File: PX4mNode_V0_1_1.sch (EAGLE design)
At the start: 128 parts, among them J201 DF13C-6P-1.25V, J202 DF13C-6P-1.25V, J203 DF13C-6P-1.25V, J301 DF13C-4P-1.25V, J401 DF13C-7P-1.25V, J402 DF13-4P-1.25V, J403 DF13C-4P-1.25V, J404 DF13C-4P-1.25V, J405 DF13C-4P-1.25V, J801 DF13C-3P-1.25V, M3_MOUNT1101 MOUNT-HOLE3.1MM, M3_MOUNT1102 MOUNT-HOLE3.1MM, M3_MOUNT1103 MOUNT-HOLE3.1MM, M3_MOUNT1104 MOUNT-HOLE3.1MM, U101 STM32F4X7VX, U401 MAX3051, U402 MAX3051, X101 3.2x2.5 mm / 24 MHz / 15 ppm

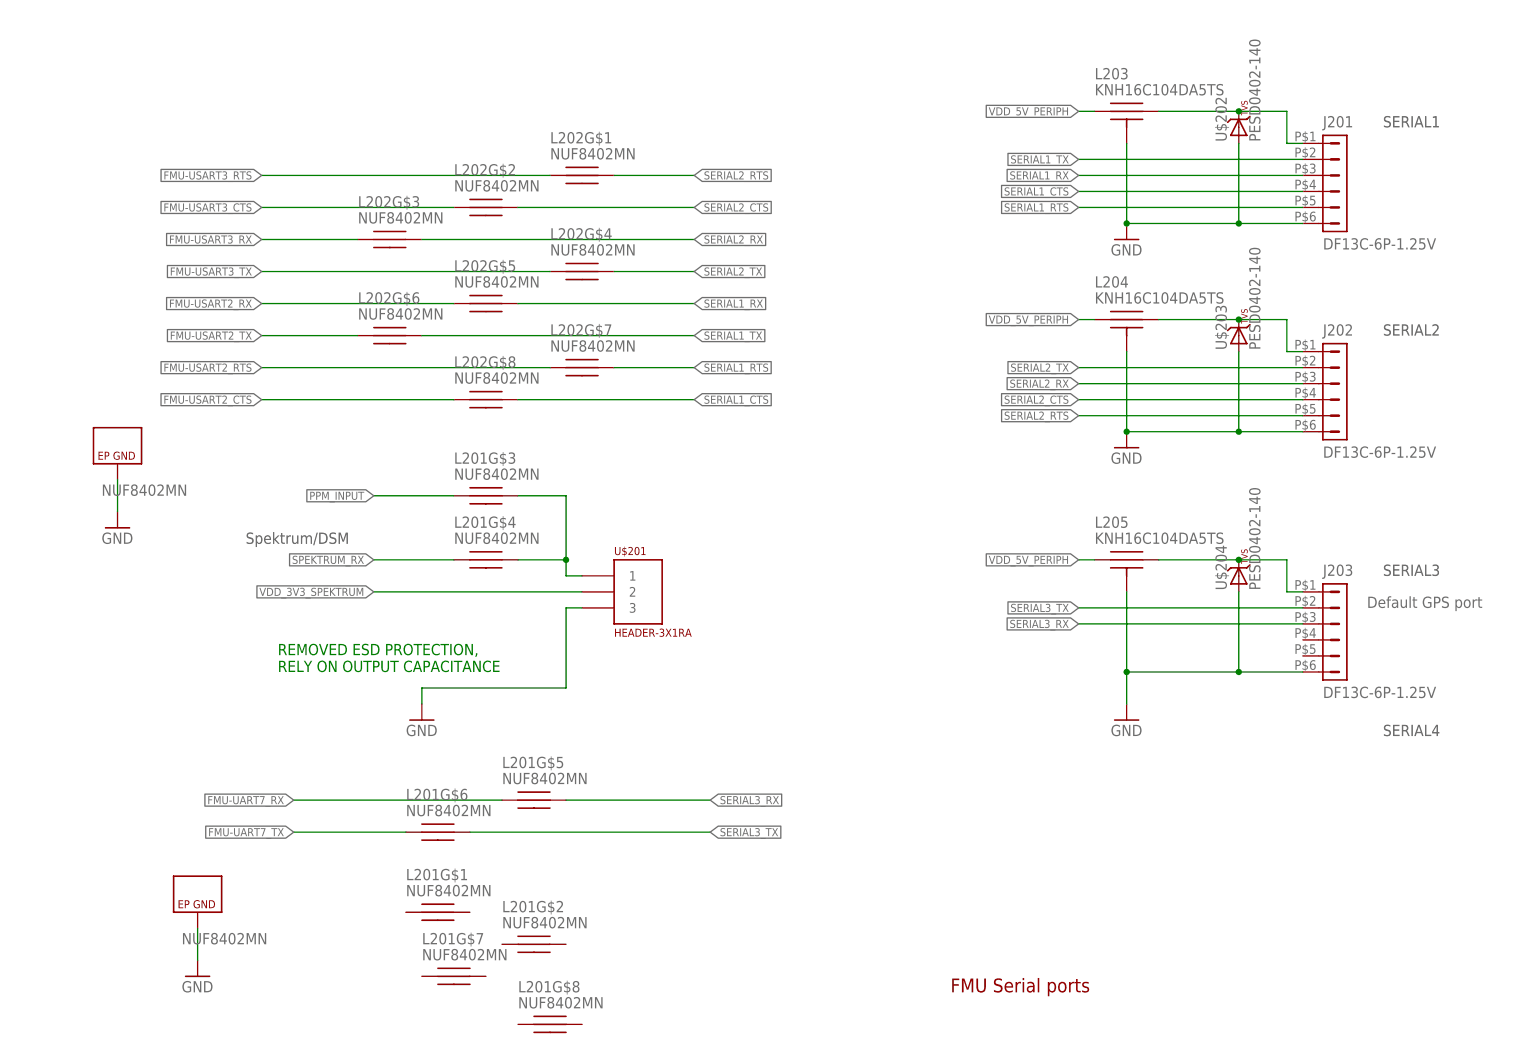
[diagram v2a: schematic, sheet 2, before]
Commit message: Added spektrum 3V3 enable signal
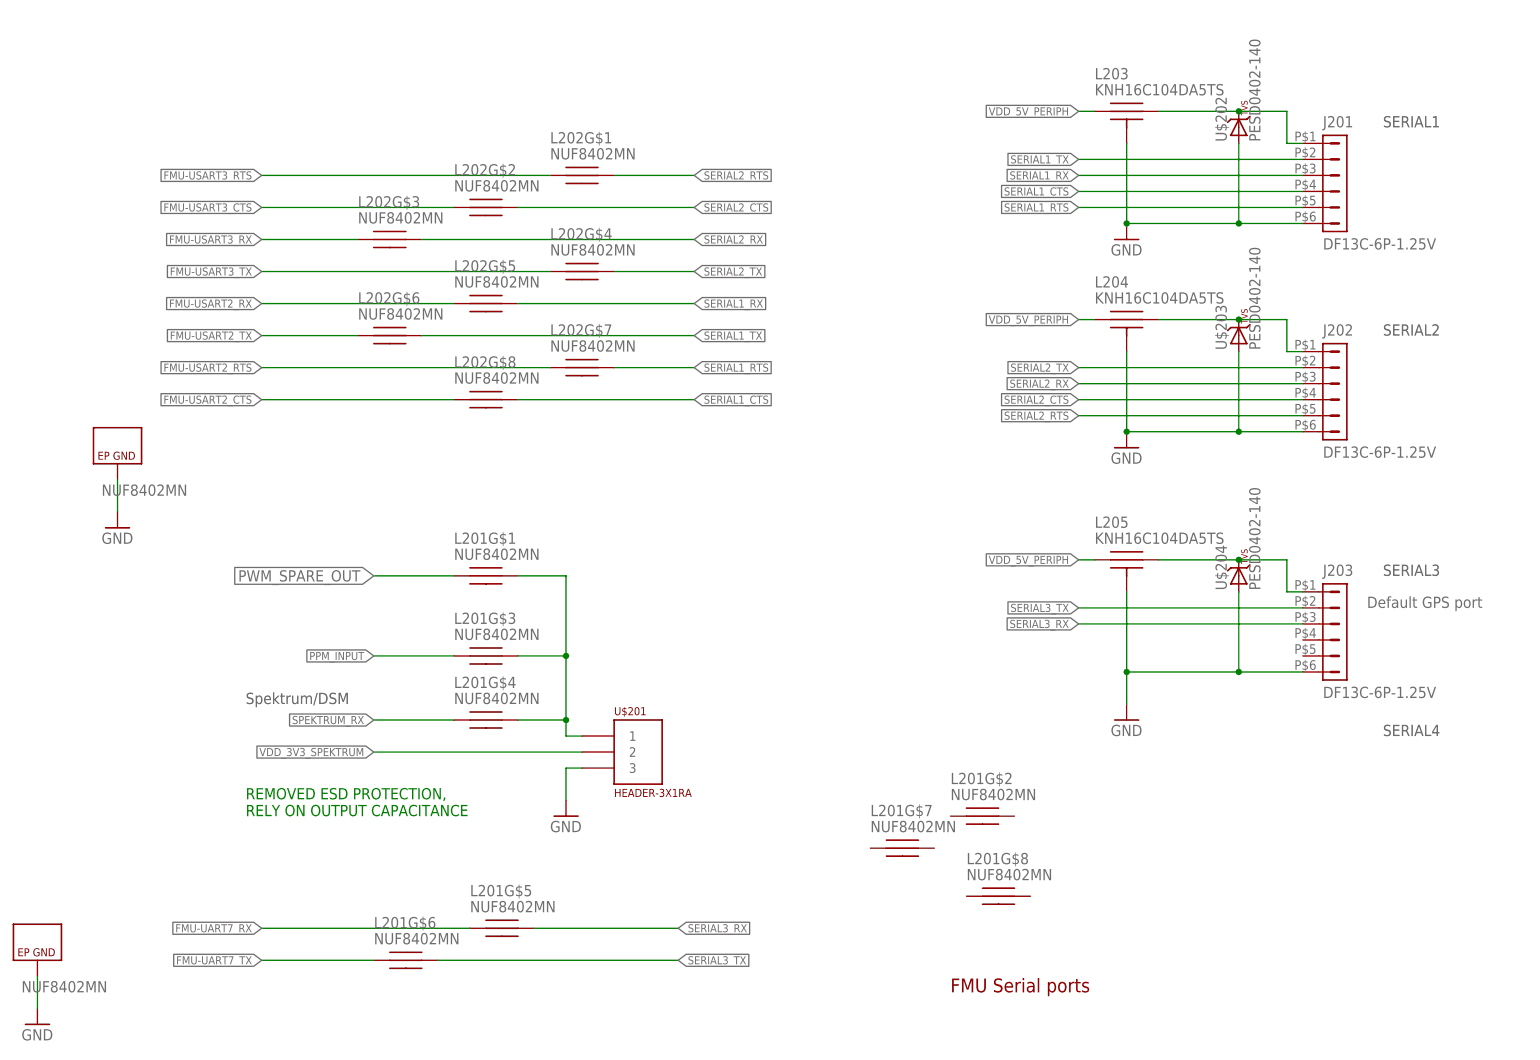
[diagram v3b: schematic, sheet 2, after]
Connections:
- removed net FMU-CH10: U101PORTA_L.PA3
- new net PWM_SPARE_OUT: L201G$1.P$1
- net N$18: now also L201G$1.P$2
- net VDD_3V3_SPEKTRUM_EN: now also U101PORTA_L.PA3
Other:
- note added: "FMU-CH10 changed to Spektrum 3v3 EN"
- moved on the sheet: L201G$1, L201G$2, L201G$3, L201G$4, L201G$5, L201G$6, L201G$7, L201G$8, U$201
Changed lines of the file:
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@@
 <text x="112.014" y="159.512" size="1.27" layer="91">Spare ADC</text>
 <text x="112.014" y="162.052" size="1.27" layer="91">Spare ADC</text>
+<text x="68.58" y="160.02" size="1.27" layer="91">FMU-CH10 changed to
+Spektrum 3v3 EN</text>
 </plain>
 <instances>
@@
 </segment>
 </net>
-<net name="FMU-CH10" class="0">
+<net name="VDD_3V3_SPEKTRUM_EN" class="0">
 <segment>
 <pinref part="U101" gate="PORTA_L" pin="PA3"/>
-<wire x1="33.02" y1="157.48" x2="53.34" y2="157.48" width="0.1524" layer="91"/>
-<label x="53.34" y="157.48" size="1.27" layer="95" xref="yes"/>
+<wire x1="33.02" y1="157.48" x2="40.64" y2="157.48" width="0.1524" layer="91"/>
+<label x="40.64" y="157.48" size="1.27" layer="95" xref="yes"/>
 </segment>
 </net>
@@
 <text x="233.68" y="58.42" size="1.778" layer="97">SERIAL4</text>
 <text x="231.14" y="78.74" size="1.778" layer="95">Default GPS port</text>
-<text x="53.34" y="88.9" size="1.778" layer="97">Spektrum/DSM</text>
-<text x="58.42" y="68.58" size="1.778" layer="91">REMOVED ESD PROTECTION,
+<text x="53.34" y="63.5" size="1.778" layer="97">Spektrum/DSM</text>
+<text x="53.34" y="45.72" size="1.778" layer="91">REMOVED ESD PROTECTION,
 RELY ON OUTPUT CAPACITANCE</text>
 </plain>
@@
 <instance part="L202" gate="G$9" x="33.02" y="99.06"/>
 <instance part="GND8" gate="1" x="33.02" y="91.44"/>
-<instance part="L201" gate="G$9" x="45.72" y="27.94"/>
-<instance part="L201" gate="G$5" x="99.06" y="48.26"/>
-<instance part="L201" gate="G$6" x="83.82" y="43.18"/>
-<instance part="L201" gate="G$3" x="91.44" y="96.52"/>
-<instance part="L201" gate="G$4" x="91.44" y="86.36"/>
-<instance part="GND9" gate="1" x="45.72" y="20.32"/>
-<instance part="GND46" gate="1" x="81.28" y="60.96"/>
-<instance part="U$201" gate="G$1" x="114.3" y="78.74"/>
-<instance part="L201" gate="G$1" x="83.82" y="30.48"/>
-<instance part="L201" gate="G$2" x="99.06" y="25.4"/>
-<instance part="L201" gate="G$7" x="86.36" y="20.32"/>
-<instance part="L201" gate="G$8" x="101.6" y="12.7"/>
+<instance part="L201" gate="G$9" x="20.32" y="20.32"/>
+<instance part="L201" gate="G$5" x="93.98" y="27.94"/>
+<instance part="L201" gate="G$6" x="78.74" y="22.86"/>
+<instance part="L201" gate="G$3" x="91.44" y="71.12"/>
+<instance part="L201" gate="G$4" x="91.44" y="60.96"/>
+<instance part="GND9" gate="1" x="20.32" y="12.7"/>
+<instance part="GND46" gate="1" x="104.14" y="45.72"/>
+<instance part="U$201" gate="G$1" x="114.3" y="53.34"/>
+<instance part="L201" gate="G$1" x="91.44" y="83.82"/>
+<instance part="L201" gate="G$2" x="170.18" y="45.72"/>
+<instance part="L201" gate="G$7" x="157.48" y="40.64"/>
+<instance part="L201" gate="G$8" x="172.72" y="33.02"/>
 </instances>
 <busses>
@@
 </segment>
 <segment>
-<label x="127" y="43.18" size="1.27" layer="95" xref="yes"/>
+<label x="121.92" y="22.86" size="1.27" layer="95" xref="yes"/>
 <pinref part="L201" gate="G$6" pin="P$2"/>
-<wire x1="127" y1="43.18" x2="88.9" y2="43.18" width="0.1524" layer="91"/>
+<wire x1="121.92" y1="22.86" x2="83.82" y2="22.86" width="0.1524" layer="91"/>
 </segment>
 </net>
@@
 </segment>
 <segment>
-<label x="127" y="48.26" size="1.27" layer="95" xref="yes"/>
+<label x="121.92" y="27.94" size="1.27" layer="95" xref="yes"/>
 <pinref part="L201" gate="G$5" pin="P$2"/>
-<wire x1="127" y1="48.26" x2="104.14" y2="48.26" width="0.1524" layer="91"/>
+<wire x1="121.92" y1="27.94" x2="99.06" y2="27.94" width="0.1524" layer="91"/>
 </segment>
 </net>
@@
 <segment>
 <pinref part="GND9" gate="1" pin="GND"/>
-<wire x1="45.72" y1="22.86" x2="45.72" y2="27.94" width="0.1524" layer="91"/>
+<wire x1="20.32" y1="15.24" x2="20.32" y2="20.32" width="0.1524" layer="91"/>
 <pinref part="L201" gate="G$9" pin="GND"/>
 </segment>
@@
 <pinref part="GND46" gate="1" pin="GND"/>
 <pinref part="U$201" gate="G$1" pin="3"/>
-<wire x1="81.28" y1="66.04" x2="81.28" y2="63.5" width="0.1524" layer="91"/>
-<wire x1="106.68" y1="78.74" x2="104.14" y2="78.74" width="0.1524" layer="91"/>
-<wire x1="104.14" y1="78.74" x2="104.14" y2="66.04" width="0.1524" layer="91"/>
-<wire x1="104.14" y1="66.04" x2="81.28" y2="66.04" width="0.1524" layer="91"/>
+<wire x1="106.68" y1="53.34" x2="104.14" y2="53.34" width="0.1524" layer="91"/>
+<wire x1="104.14" y1="53.34" x2="104.14" y2="48.26" width="0.1524" layer="91"/>
 </segment>
 </net>
@@
 <net name="SPEKTRUM_RX" class="0">
 <segment>
-<label x="73.66" y="86.36" size="1.27" layer="95" font="vector" rot="R180" xref="yes"/>
-<wire x1="86.36" y1="86.36" x2="73.66" y2="86.36" width="0.1524" layer="91"/>
+<label x="73.66" y="60.96" size="1.27" layer="95" font="vector" rot="R180" xref="yes"/>
+<wire x1="86.36" y1="60.96" x2="73.66" y2="60.96" width="0.1524" layer="91"/>
 <pinref part="L201" gate="G$4" pin="P$1"/>
 </segment>
@@
 <net name="VDD_3V3_SPEKTRUM" class="1">
 <segment>
-<label x="73.66" y="81.28" size="1.27" layer="95" rot="R180" xref="yes"/>
+<label x="73.66" y="55.88" size="1.27" layer="95" rot="R180" xref="yes"/>
 <pinref part="U$201" gate="G$1" pin="2"/>
-<wire x1="106.68" y1="81.28" x2="73.66" y2="81.28" width="0.1524" layer="91"/>
+<wire x1="106.68" y1="55.88" x2="73.66" y2="55.88" width="0.1524" layer="91"/>
 </segment>
 </net>
@@
 <segment>
 <pinref part="L201" gate="G$4" pin="P$2"/>
-<wire x1="96.52" y1="86.36" x2="104.14" y2="86.36" width="0.1524" layer="91"/>
+<wire x1="96.52" y1="60.96" x2="104.14" y2="60.96" width="0.1524" layer="91"/>
 <pinref part="L201" gate="G$3" pin="P$2"/>
-<wire x1="96.52" y1="96.52" x2="104.14" y2="96.52" width="0.1524" layer="91"/>
-<wire x1="104.14" y1="96.52" x2="104.14" y2="86.36" width="0.1524" layer="91"/>
+<wire x1="96.52" y1="71.12" x2="104.14" y2="71.12" width="0.1524" layer="91"/>
+<wire x1="104.14" y1="71.12" x2="104.14" y2="60.96" width="0.1524" layer="91"/>
 <pinref part="U$201" gate="G$1" pin="1"/>
-<wire x1="106.68" y1="83.82" x2="104.14" y2="83.82" width="0.1524" layer="91"/>
-<wire x1="104.14" y1="83.82" x2="104.14" y2="86.36" width="0.1524" layer="91"/>
-<junction x="104.14" y="86.36"/>
+<wire x1="106.68" y1="58.42" x2="104.14" y2="58.42" width="0.1524" layer="91"/>
+<wire x1="104.14" y1="58.42" x2="104.14" y2="60.96" width="0.1524" layer="91"/>
+<junction x="104.14" y="60.96"/>
+<pinref part="L201" gate="G$1" pin="P$2"/>
+<wire x1="96.52" y1="83.82" x2="104.14" y2="83.82" width="0.1524" layer="91"/>
+<wire x1="104.14" y1="83.82" x2="104.14" y2="71.12" width="0.1524" layer="91"/>
+<junction x="104.14" y="71.12"/>
 </segment>
 </net>
 <net name="PPM_INPUT" class="0">
 <segment>
-<label x="73.66" y="96.52" size="1.27" layer="95" rot="R180" xref="yes"/>
-<wire x1="73.66" y1="96.52" x2="86.36" y2="96.52" width="0.1524" layer="91"/>
+<label x="73.66" y="71.12" size="1.27" layer="95" rot="R180" xref="yes"/>
+<wire x1="73.66" y1="71.12" x2="86.36" y2="71.12" width="0.1524" layer="91"/>
 <pinref part="L201" gate="G$3" pin="P$1"/>
 </segment>
@@
 <net name="FMU-UART7_RX" class="0">
 <segment>
-<label x="60.96" y="48.26" size="1.27" layer="95" rot="R180" xref="yes"/>
+<label x="55.88" y="27.94" size="1.27" layer="95" rot="R180" xref="yes"/>
 <pinref part="L201" gate="G$5" pin="P$1"/>
-<wire x1="60.96" y1="48.26" x2="93.98" y2="48.26" width="0.1524" layer="91"/>
+<wire x1="55.88" y1="27.94" x2="88.9" y2="27.94" width="0.1524" layer="91"/>
 </segment>
 </net>
 <net name="FMU-UART7_TX" class="0">
 <segment>
-<label x="60.96" y="43.18" size="1.27" layer="95" rot="R180" xref="yes"/>
+<label x="55.88" y="22.86" size="1.27" layer="95" rot="R180" xref="yes"/>
 <pinref part="L201" gate="G$6" pin="P$1"/>
-<wire x1="78.74" y1="43.18" x2="60.96" y2="43.18" width="0.1524" layer="91"/>
+<wire x1="73.66" y1="22.86" x2="55.88" y2="22.86" width="0.1524" layer="91"/>
+</segment>
+</net>
+<net name="PWM_SPARE_OUT" class="0">
+<segment>
+<pinref part="L201" gate="G$1" pin="P$1"/>
+<wire x1="86.36" y1="83.82" x2="73.66" y2="83.82" width="0.1524" layer="91"/>
+<label x="73.66" y="83.82" size="1.778" layer="95" rot="R180" xref="yes"/>
 </segment>
 </net>
@@
 <net name="VDD_3V3_SPEKTRUM_EN" class="0">
 <segment>
-<wire x1="40.64" y1="165.1" x2="121.92" y2="165.1" width="0.1524" layer="91"/>
-<label x="121.92" y="165.1" size="1.27" layer="95" xref="yes"/>
+<wire x1="40.64" y1="165.1" x2="33.02" y2="165.1" width="0.1524" layer="91"/>
+<label x="33.02" y="165.1" size="1.27" layer="95" rot="R180" xref="yes"/>
 <pinref part="R701" gate="G$1" pin="2"/>
 <wire x1="40.64" y1="165.1" x2="40.64" y2="149.86" width="0.1524" layer="91"/>

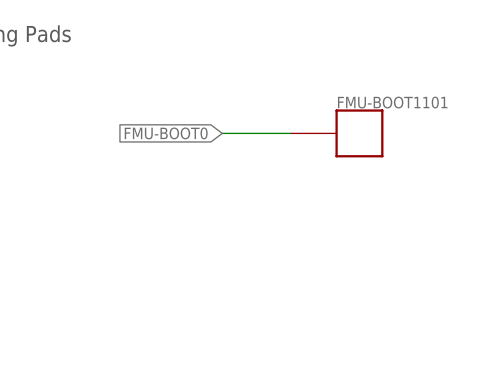
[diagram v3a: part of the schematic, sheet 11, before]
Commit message: Moved boot pad to safer position
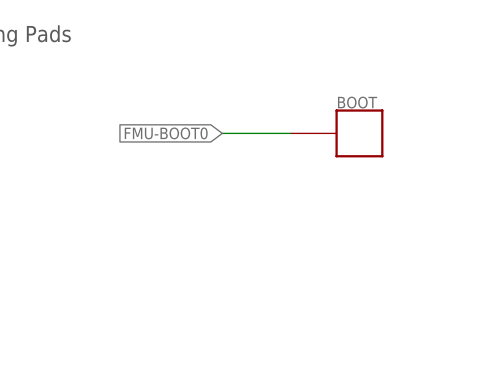
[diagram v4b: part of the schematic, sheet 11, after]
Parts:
- renumbered FMU-BOOT1101 to BOOT
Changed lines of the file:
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@@
 </part>
 <part name="GND35" library="pixhawk2" deviceset="GND" device=""/>
-<part name="FMU-BOOT1101" library="pixhawk2" deviceset="PAD" device=".04">
+<part name="BOOT" library="pixhawk2" deviceset="PAD" device=".04">
 <attribute name="BOM" value="EXCLUDE"/>
 <attribute name="PARTNO" value="*"/>
@@
 <attribute name="BOM" x="71.12" y="132.08" size="1.778" layer="96" display="off"/>
 </instance>
-<instance part="FMU-BOOT1101" gate="G$1" x="231.14" y="160.02">
+<instance part="BOOT" gate="G$1" x="231.14" y="160.02">
 <attribute name="PARTNO" x="231.14" y="160.02" size="1.778" layer="96" display="off"/>
 <attribute name="BOM" x="231.14" y="160.02" size="1.778" layer="96" display="off"/>
@@
 <wire x1="223.52" y1="160.02" x2="215.9" y2="160.02" width="0.1524" layer="91"/>
 <label x="215.9" y="160.02" size="1.27" layer="95" rot="R180" xref="yes"/>
-<pinref part="FMU-BOOT1101" gate="G$1" pin="P$1"/>
+<pinref part="BOOT" gate="G$1" pin="P$1"/>
 </segment>
 </net>

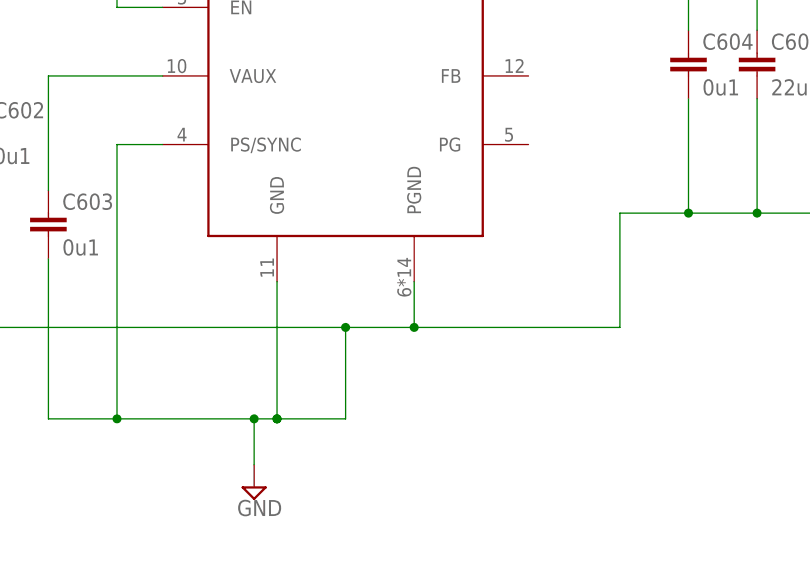
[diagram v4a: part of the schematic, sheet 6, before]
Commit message: Modified EP solder paste masks with crosshatch to reduce solder voids
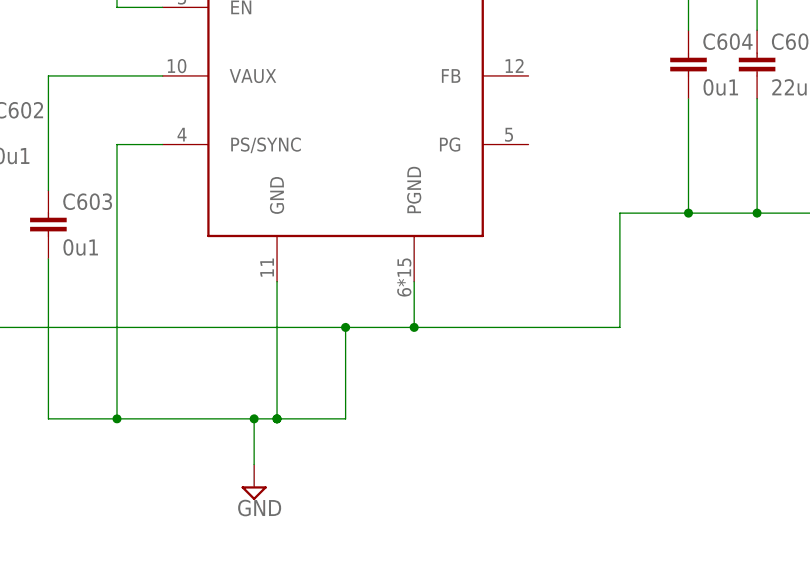
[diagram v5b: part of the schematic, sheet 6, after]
